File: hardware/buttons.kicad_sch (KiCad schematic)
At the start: 9 parts

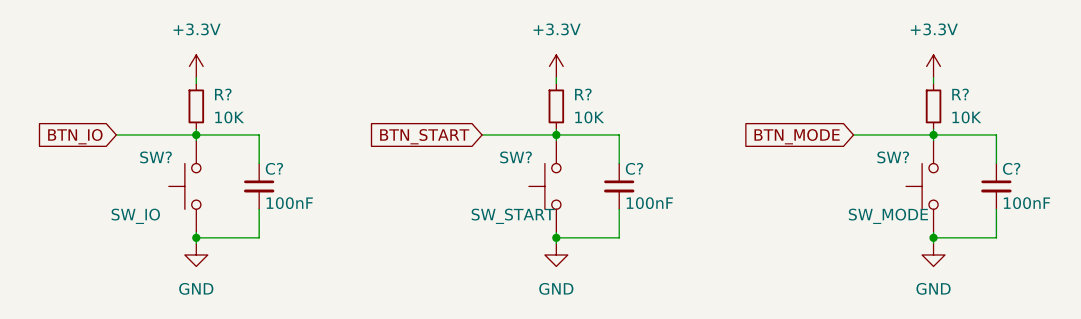
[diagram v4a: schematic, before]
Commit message: Schematics are completed
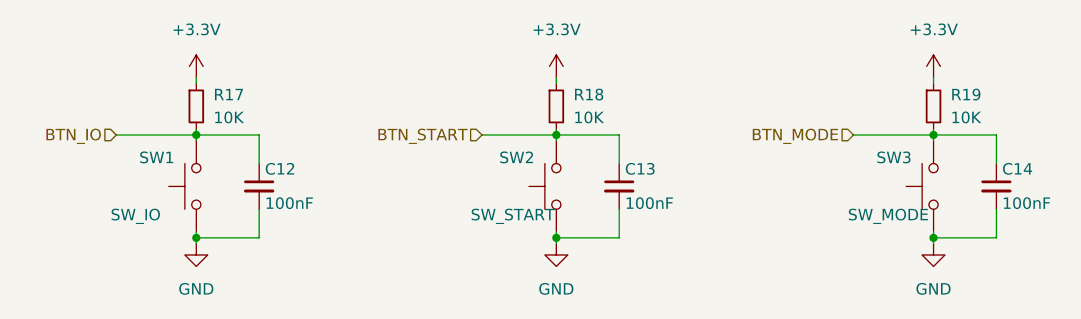
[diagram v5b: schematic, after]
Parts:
- C12, C13, C14: renamed from C?; footprint (none) -> Capacitor_SMD:C_0603_1608Metric
- R17, R18, R19: renamed from R?; footprint (none) -> Resistor_SMD:R_0603_1608Metric
- SW1, SW2, SW3: renamed from SW?; footprint (none) -> Button_Switch_THT:SW_PUSH-12mm
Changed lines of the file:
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@@
     (stroke (width 0) (type default) (color 0 0 0 0))
   )
-  (global_label "BTN_IO" (shape input) (at 99.695 95.25 180) (fields_autoplaced)
+  (hierarchical_label "BTN_MODE" (shape input) (at 181.61 95.25 180)
     (effects (font (size 1.27 1.27)) (justify right))
-    (property "Intersheet References" "${INTERSHEET_REFS}" (id 0) (at 90.8109 95.1706 0)
-      (effects (font (size 1.27 1.27)) (justify right) hide)
-    )
-  )
-  (global_label "BTN_MODE" (shape input) (at 181.61 95.25 180) (fields_autoplaced)
+  )
+  (hierarchical_label "BTN_IO" (shape input) (at 99.695 95.25 180)
     (effects (font (size 1.27 1.27)) (justify right))
-    (property "Intersheet References" "${INTERSHEET_REFS}" (id 0) (at 169.4602 95.1706 0)
-      (effects (font (size 1.27 1.27)) (justify right) hide)
-    )
-  )
-  (global_label "BTN_START" (shape input) (at 140.335 95.25 180) (fields_autoplaced)
+  )
+  (hierarchical_label "BTN_START" (shape input) (at 140.335 95.25 180)
     (effects (font (size 1.27 1.27)) (justify right))
-    (property "Intersheet References" "${INTERSHEET_REFS}" (id 0) (at 127.8829 95.1706 0)
-      (effects (font (size 1.27 1.27)) (justify right) hide)
-    )
   )
   (symbol (lib_id "power:GND") (at 148.59 107.315 0) (unit 1)
     (in_bom yes) (on_board yes) (fields_autoplaced)
-    (property "Reference" "#PWR?" (id 0) (at 148.59 113.665 0)
+    (property "Reference" "#PWR027" (id 0) (at 148.59 113.665 0)
       (effects (font (size 1.27 1.27)) hide)
     )
@@
   (symbol (lib_id "Switch:SW_Push") (at 148.59 100.965 90) (unit 1)
     (in_bom yes) (on_board yes)
-    (property "Reference" "SW?" (id 0) (at 142.24 97.79 90)
+    (property "Reference" "SW2" (id 0) (at 142.24 97.79 90)
       (effects (font (size 1.27 1.27)) (justify right))
     )
@@
       (effects (font (size 1.27 1.27)) (justify right))
     )
-    (property "Footprint" "" (id 2) (at 143.51 100.965 0)
+    (property "Footprint" "Button_Switch_THT:SW_PUSH-12mm" (id 2) (at 143.51 100.965 0)
       (effects (font (size 1.27 1.27)) hide)
     )
@@
   (symbol (lib_id "power:GND") (at 190.5 107.315 0) (unit 1)
     (in_bom yes) (on_board yes) (fields_autoplaced)
-    (property "Reference" "#PWR?" (id 0) (at 190.5 113.665 0)
+    (property "Reference" "#PWR029" (id 0) (at 190.5 113.665 0)
       (effects (font (size 1.27 1.27)) hide)
     )
@@
   (symbol (lib_id "Device:R_Small") (at 190.5 92.075 0) (unit 1)
     (in_bom yes) (on_board yes) (fields_autoplaced)
-    (property "Reference" "R?" (id 0) (at 192.405 90.8049 0)
+    (property "Reference" "R19" (id 0) (at 192.405 90.8049 0)
       (effects (font (size 1.27 1.27)) (justify left))
     )
@@
       (effects (font (size 1.27 1.27)) (justify left))
     )
-    (property "Footprint" "" (id 2) (at 190.5 92.075 0)
+    (property "Footprint" "Resistor_SMD:R_0603_1608Metric" (id 2) (at 190.5 92.075 0)
       (effects (font (size 1.27 1.27)) hide)
     )
@@
   (symbol (lib_id "power:+3.3V") (at 190.5 88.9 0) (unit 1)
     (in_bom yes) (on_board yes) (fields_autoplaced)
-    (property "Reference" "#PWR?" (id 0) (at 190.5 92.71 0)
+    (property "Reference" "#PWR028" (id 0) (at 190.5 92.71 0)
       (effects (font (size 1.27 1.27)) hide)
     )
@@
   (symbol (lib_id "power:GND") (at 108.585 107.315 0) (unit 1)
     (in_bom yes) (on_board yes) (fields_autoplaced)
-    (property "Reference" "#PWR?" (id 0) (at 108.585 113.665 0)
+    (property "Reference" "#PWR025" (id 0) (at 108.585 113.665 0)
       (effects (font (size 1.27 1.27)) hide)
     )
@@
   (symbol (lib_id "power:+3.3V") (at 108.585 88.9 0) (unit 1)
     (in_bom yes) (on_board yes) (fields_autoplaced)
-    (property "Reference" "#PWR?" (id 0) (at 108.585 92.71 0)
+    (property "Reference" "#PWR024" (id 0) (at 108.585 92.71 0)
       (effects (font (size 1.27 1.27)) hide)
     )
@@
   (symbol (lib_id "power:+3.3V") (at 148.59 88.9 0) (unit 1)
     (in_bom yes) (on_board yes) (fields_autoplaced)
-    (property "Reference" "#PWR?" (id 0) (at 148.59 92.71 0)
+    (property "Reference" "#PWR026" (id 0) (at 148.59 92.71 0)
       (effects (font (size 1.27 1.27)) hide)
     )
@@
   (symbol (lib_id "Switch:SW_Push") (at 190.5 100.965 90) (unit 1)
     (in_bom yes) (on_board yes)
-    (property "Reference" "SW?" (id 0) (at 184.15 97.79 90)
+    (property "Reference" "SW3" (id 0) (at 184.15 97.79 90)
       (effects (font (size 1.27 1.27)) (justify right))
     )
@@
       (effects (font (size 1.27 1.27)) (justify right))
     )
-    (property "Footprint" "" (id 2) (at 185.42 100.965 0)
+    (property "Footprint" "Button_Switch_THT:SW_PUSH-12mm" (id 2) (at 185.42 100.965 0)
       (effects (font (size 1.27 1.27)) hide)
     )
@@
   (symbol (lib_id "Device:R_Small") (at 108.585 92.075 0) (unit 1)
     (in_bom yes) (on_board yes) (fields_autoplaced)
-    (property "Reference" "R?" (id 0) (at 110.49 90.8049 0)
+    (property "Reference" "R17" (id 0) (at 110.49 90.8049 0)
       (effects (font (size 1.27 1.27)) (justify left))
     )
@@
       (effects (font (size 1.27 1.27)) (justify left))
     )
-    (property "Footprint" "" (id 2) (at 108.585 92.075 0)
+    (property "Footprint" "Resistor_SMD:R_0603_1608Metric" (id 2) (at 108.585 92.075 0)
       (effects (font (size 1.27 1.27)) hide)
     )
@@
   (symbol (lib_id "Device:C_Small") (at 115.57 100.965 0) (unit 1)
     (in_bom yes) (on_board yes)
-    (property "Reference" "C?" (id 0) (at 116.205 99.06 0)
+    (property "Reference" "C12" (id 0) (at 116.205 99.06 0)
       (effects (font (size 1.27 1.27)) (justify left))
     )
@@
       (effects (font (size 1.27 1.27)) (justify left))
     )
-    (property "Footprint" "" (id 2) (at 115.57 100.965 0)
+    (property "Footprint" "Capacitor_SMD:C_0603_1608Metric" (id 2) (at 115.57 100.965 0)
       (effects (font (size 1.27 1.27)) hide)
     )
@@
   (symbol (lib_id "Device:C_Small") (at 197.485 100.965 0) (unit 1)
     (in_bom yes) (on_board yes)
-    (property "Reference" "C?" (id 0) (at 198.12 99.06 0)
+    (property "Reference" "C14" (id 0) (at 198.12 99.06 0)
       (effects (font (size 1.27 1.27)) (justify left))
     )
@@
       (effects (font (size 1.27 1.27)) (justify left))
     )
-    (property "Footprint" "" (id 2) (at 197.485 100.965 0)
+    (property "Footprint" "Capacitor_SMD:C_0603_1608Metric" (id 2) (at 197.485 100.965 0)
       (effects (font (size 1.27 1.27)) hide)
     )
@@
   (symbol (lib_id "Device:C_Small") (at 155.575 100.965 0) (unit 1)
     (in_bom yes) (on_board yes)
-    (property "Reference" "C?" (id 0) (at 156.21 99.06 0)
+    (property "Reference" "C13" (id 0) (at 156.21 99.06 0)
       (effects (font (size 1.27 1.27)) (justify left))
     )
@@
       (effects (font (size 1.27 1.27)) (justify left))
     )
-    (property "Footprint" "" (id 2) (at 155.575 100.965 0)
+    (property "Footprint" "Capacitor_SMD:C_0603_1608Metric" (id 2) (at 155.575 100.965 0)
       (effects (font (size 1.27 1.27)) hide)
     )
@@
   (symbol (lib_id "Device:R_Small") (at 148.59 92.075 0) (unit 1)
     (in_bom yes) (on_board yes) (fields_autoplaced)
-    (property "Reference" "R?" (id 0) (at 150.495 90.8049 0)
+    (property "Reference" "R18" (id 0) (at 150.495 90.8049 0)
       (effects (font (size 1.27 1.27)) (justify left))
     )
@@
       (effects (font (size 1.27 1.27)) (justify left))
     )
-    (property "Footprint" "" (id 2) (at 148.59 92.075 0)
+    (property "Footprint" "Resistor_SMD:R_0603_1608Metric" (id 2) (at 148.59 92.075 0)
       (effects (font (size 1.27 1.27)) hide)
     )
@@
   (symbol (lib_id "Switch:SW_Push") (at 108.585 100.965 90) (unit 1)
     (in_bom yes) (on_board yes)
-    (property "Reference" "SW?" (id 0) (at 102.235 97.79 90)
+    (property "Reference" "SW1" (id 0) (at 102.235 97.79 90)
       (effects (font (size 1.27 1.27)) (justify right))
     )
@@
       (effects (font (size 1.27 1.27)) (justify right))
     )
-    (property "Footprint" "" (id 2) (at 103.505 100.965 0)
-      (effects (font (size 1.27 1.27)) hide)
-    )
+    (property "Footprint" "Button_Switch_THT:SW_PUSH-12mm" (id 2) (at 103.505 100.965 0)
+      (effects (font (size 1.27 1.27)) hide)
+    )

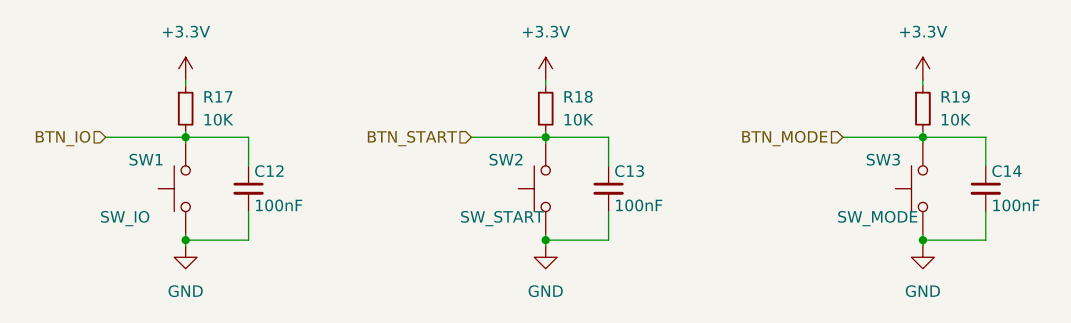
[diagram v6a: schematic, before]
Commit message: Footprints are assigned and Cut edges fixed
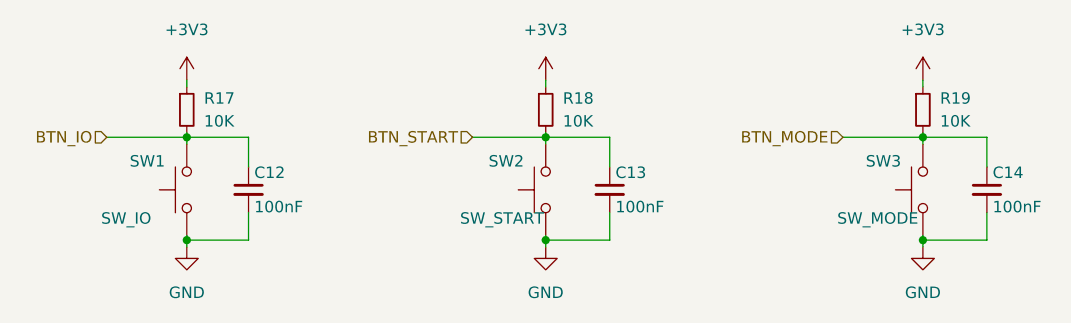
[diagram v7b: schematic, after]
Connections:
- net +3.3V renamed +3V3
